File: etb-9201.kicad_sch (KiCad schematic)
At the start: 5 parts, among them U36 TLE9201SG

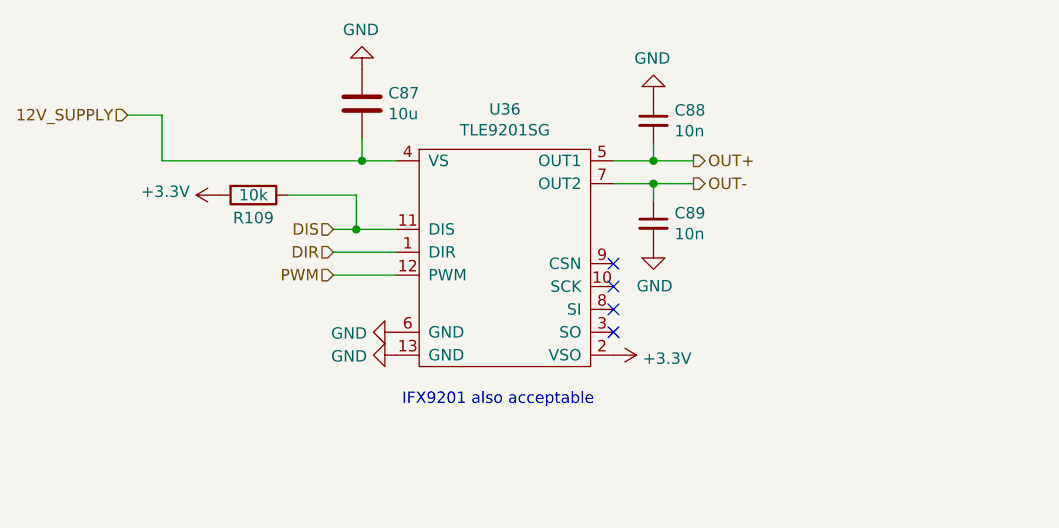
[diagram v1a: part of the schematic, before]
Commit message: Updates - Route digital inputs to connector - Add optional VR conditioner - Second Enable for H-Bridge
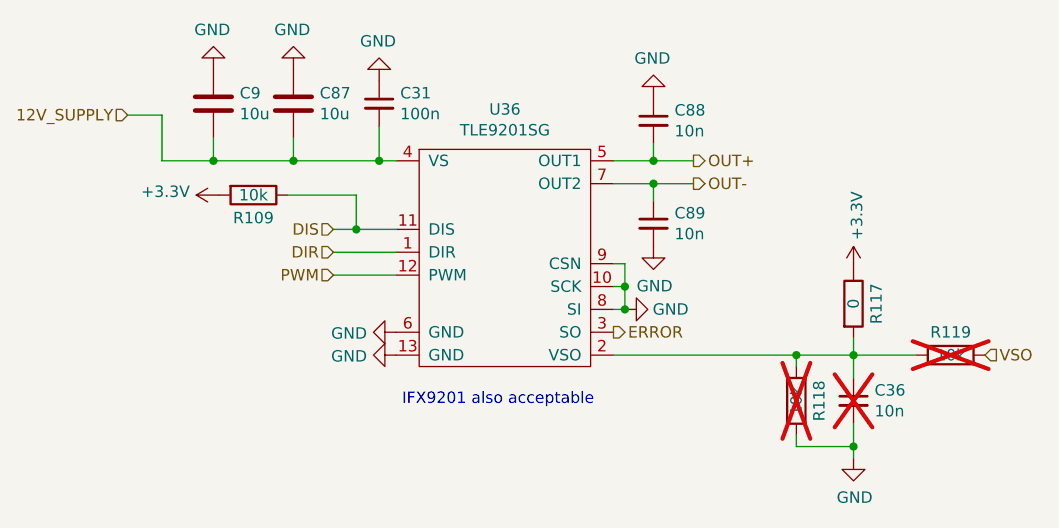
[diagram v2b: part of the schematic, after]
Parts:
- added C31: 100n, Capacitor_SMD:C_0603_1608Metric, symbol Device:C_Small
- added C36: 10n, Capacitor_SMD:C_0603_1608Metric, symbol Device:C_Small
- added C9: 10u, Capacitor_SMD:C_1206_3216Metric, symbol Device:C
- added R117: 0, Resistor_SMD:R_0402_1005Metric, symbol Device:R
- added R118, R119: 10k, Resistor_SMD:R_0402_1005Metric, symbol Device:R
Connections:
- net +3V3: now also R117.1; no longer U36.2 (VSO)
- net 12V_SUPPLY: now also C31.2, C9.2
- net GND: now also U36.10 (SCK), U36.8 (SI), U36.9 (CSN), C31.1, C36.2, C9.1, R118.2
- net ERROR: now reaches U36.3 (SO)
- new net: C36.1, R117.2, R118.1, R119.1, U36.2 (VSO)
- new net VSO: R119.2
- no-connect marks 4 -> 0
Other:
- moved on the sheet: C87

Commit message: USB jack, parts and LCSC numbers, headphone jack
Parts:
- R117: LCSC C25744 -> C60485
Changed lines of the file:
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@@
       (effects (font (size 1.27 1.27)) hide)
     )
-    (property "LCSC" "C25744" (at 111.125 48.895 0)
+    (property "LCSC" "C60485" (at 111.125 48.895 0)
       (effects (font (size 1.27 1.27)) hide)
     )

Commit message: Several optimizations
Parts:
- added C90, C91: 10u, Capacitor_SMD:C_1206_3216Metric, symbol Device:C
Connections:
- net 12V_SUPPLY: now also C90.2, C91.2
- net GND: now also C90.1, C91.1
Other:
- moved on the sheet: C31, C36, C87, C88, C89, C9, R109, R117, R118, R119, U36

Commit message: Fix connector, optimize psu
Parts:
- U36: footprint Package_SO:Infineon_PG-DSO-12-9 -> Package_SO:Infineon_PG-DSO-12-9_ThermalVias
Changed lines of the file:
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@@
       (effects (font (size 1.27 1.27)))
     )
-    (property "Footprint" "Package_SO:Infineon_PG-DSO-12-9" (at 75.565 41.91 0)
+    (property "Footprint" "Package_SO:Infineon_PG-DSO-12-9_ThermalVias" (at 75.565 41.91 0)
       (effects (font (size 1.27 1.27)) hide)
     )

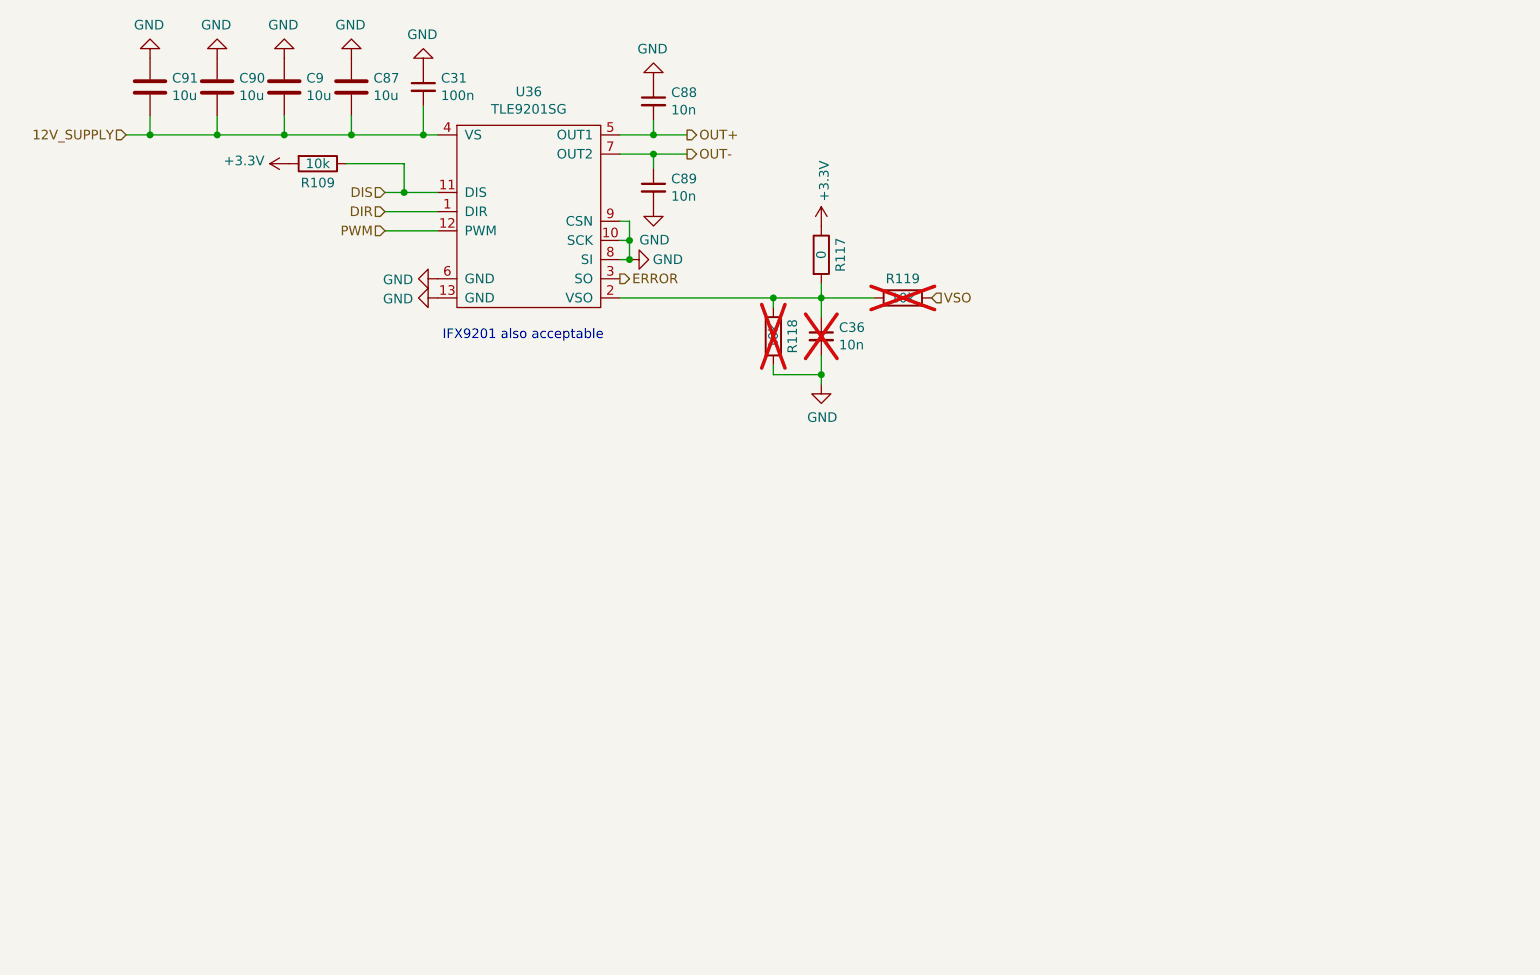
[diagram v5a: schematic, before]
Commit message: Add Stepper, fix Connector, add Testpoints, several changes
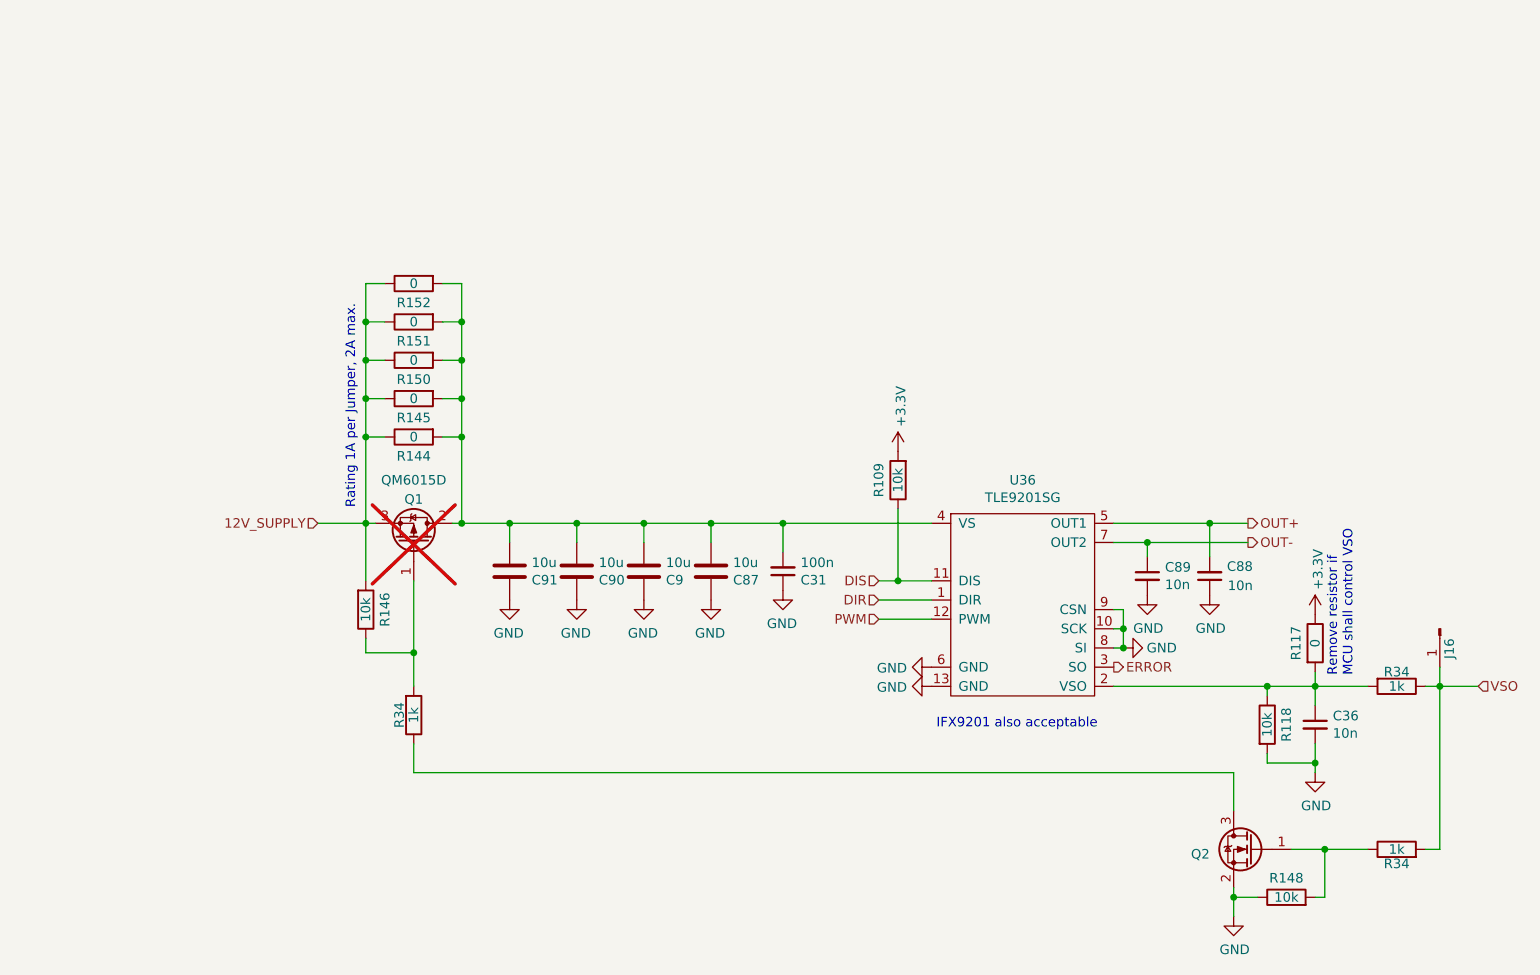
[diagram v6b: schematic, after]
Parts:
- removed R119: 10k, Resistor_SMD:R_0402_1005Metric, symbol Device:R
- added J16: Conn_01x01_Pin, Connector_PinHeader_2.54mm:PinHeader_1x01_P2.54mm_Vertical, symbol Connector:Conn_01x01_Pin
- added Q1: QM6015D, Package_TO_SOT_SMD:TO-252-2, symbol Transistor_FET:QM6015D
- added Q2: 2N7002, Package_TO_SOT_SMD:SOT-23, symbol Transistor_FET:2N7002
- added R144, R145, R150, R151, R152: 0, Resistor_SMD:R_0402_1005Metric, symbol Device:R
- added R146, R148: 10k, Resistor_SMD:R_0402_1005Metric, symbol Device:R
- added R34 (x3): 1k, Resistor_SMD:R_0402_1005Metric, symbol Device:R
- C36, R118: now fitted
- R117: LCSC C60485 -> C17168
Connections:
- net 12V_SUPPLY: now also Q1.3 (S), R144.1, R145.1, R146.2, R150.1, R151.1, R152.1; no longer C31.2, C87.2, C9.2, C90.2, C91.2, U36.4 (VS)
- net GND: now also Q2.2 (S), R148.1
- net VSO: now also J16.1 (Pin_1), R34.1, R34.2
- net at C36.1, R117.2, R118.1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: now also R34.2
- new net: C31.2, C87.2, C9.2, C90.2, C91.2, Q1.2 (D), R144.2, R145.2, R150.2, R151.2, R152.2, U36.4 (VS)
- new net: Q2.3 (D), R34.1
- new net: Q1.1 (G), R146.1, R34.2
- new net: Q2.1 (G), R148.2, R34.1
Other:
- note added: "Rating 1A per Jumper, 2A max."
- note added: "Remove resistor if MCU shall control VSO"
- moved on the sheet: C31, C87, C88, C89, C9, C90, C91, R109, R117, U36

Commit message: Optimize
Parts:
- removed J16: Conn_01x01_Pin, Connector_PinHeader_2.54mm:PinHeader_1x01_P2.54mm_Vertical, symbol Connector:Conn_01x01_Pin
- C31: LCSC C57112 -> C14663
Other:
- note added: "Remove jumper and assemble Q1 if MCU shall control supply"
- note added: "Remove jumper if MCU shall control VSO"
- note removed: "Remove resistor if MCU shall control VSO"
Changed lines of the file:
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@@
-    (stroke (width 0) (type default))
-  )
-  (wire (pts (xy 199.39 103.505) (xy 199.39 106.045))
     (stroke (width 0) (type default))
   )
@@
   (wire (pts (xy 199.39 106.045) (xy 204.47 106.045))
     (stroke (width 0) (type default))
+  )
+  (text "Remove jumper and assemble Q1 if\nMCU shall control supply"
+    (at 74.295 81.915 90)
+    (effects (font (size 1.27 1.27)) (justify left bottom))
   )
   (text "IFX9201 also acceptable" (at 132.715 111.76 0)
@@
     (effects (font (size 1.27 1.27)) (justify left bottom))
   )
-  (text "Remove resistor if\nMCU shall control VSO" (at 187.96 104.775 90)
+  (text "Remove jumper if\nMCU shall control VSO" (at 187.96 104.775 90)
     (effects (font (size 1.27 1.27)) (justify left bottom))
   )
@@
       (effects (font (size 1.27 1.27)) hide)
     )
-    (property "LCSC" "C57112" (at 112.395 90.805 0)
+    (property "LCSC" "C14663" (at 112.395 90.805 0)
       (effects (font (size 1.27 1.27)) hide)
     )
@@
         )
       )
-    )
-  )
-  (symbol (lib_id "Connector:Conn_01x01_Pin") (at 199.39 98.425 270) (unit 1)
-    (in_bom no) (on_board yes) (dnp no)
-    (property "Reference" "J16" (at 200.66 99.695 0)
-      (effects (font (size 1.27 1.27)) (justify left))
-    )
-    (property "Value" "Conn_01x01_Pin" (at 200.66 100.965 90)
-      (effects (font (size 1.27 1.27)) (justify left) hide)
-    )
-    (property "Footprint" "Connector_PinHeader_2.54mm:PinHeader_1x01_P2.54mm_Vertical" (at 199.39 98.425 0)
-      (effects (font (size 1.27 1.27)) hide)
-    )
-    (property "Datasheet" "~" (at 199.39 98.425 0)
-      (effects (font (size 1.27 1.27)) hide)
-    )
-    (pin "1")
-    (instances
-      (project "proteus"
-        (path "/d9116601-cae2-4199-827b-70fa136aae51/00000000-0000-0000-0000-000062471bcf"
-          (reference "J16") (unit 1)
-        )
-      )
